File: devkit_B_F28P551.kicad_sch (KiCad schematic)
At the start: 27 parts, among them J1 DEVKIT_C2000_ROW_A, J2 DEVKIT_C2000_ROW_B, J3 Tag-Connect-2050_10, J4 RESET, U1 TMS320F28P551SG5PM, U2 MCP1700-3302E/TT, U3 MCP1700-3302E/TT

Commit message: Devkit B routé, sérigraphie des connecteurs 2x28 et logo
Placement/routage complet du PCB devkit B (24 empreintes, J1/J2 câblés).
Étiquettes de sérigraphie ajoutées sur les 56 broches des connecteurs
Row A/Row B (canal ADC réel, GPIO, rôle de bus générique, alimentations)
via kipy sur l'instance ouverte, plutôt que les noms spécialisés du
schéma. Logo ajouté (lib/lebel-logo) et fp-lib-table versionné.

Co-Authored-By: Claude Sonnet 5 <noreply@anthropic.com>
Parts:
- removed C7: 2u2, Capacitor_SMD:C_0805_2012Metric, symbol Device:C
- removed C9: 100n, Capacitor_SMD:C_0805_2012Metric, symbol Device:C
- renumbered J3 to JTAG1
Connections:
- net GND: now also J1.1 (GND), J1.10 (GND), J1.13 (GND), J1.16 (GND), J1.19 (GND), J1.21 (GND), J1.23 (GND), J1.4 (GND), J1.7 (GND), J2.1 (GND), J2.14 (GND), J2.9 (GND)
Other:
- moved on the sheet: C1, C10, C11, C12, C13, C14, C2, C3, C4, C5, C6, C8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

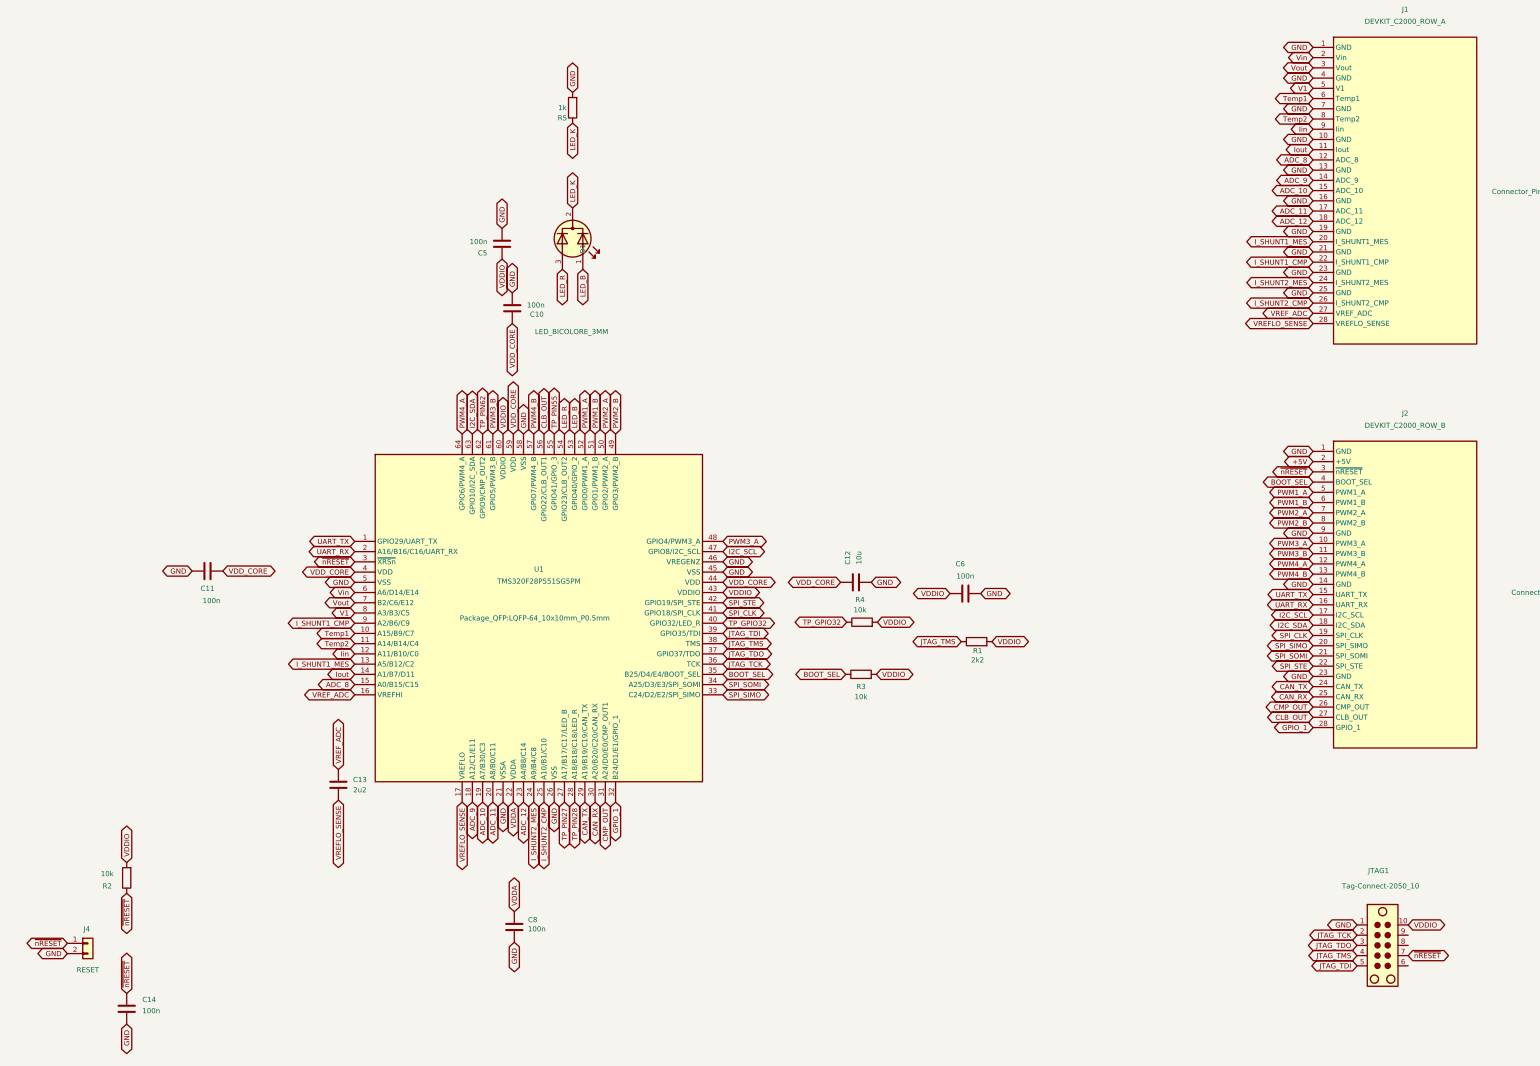
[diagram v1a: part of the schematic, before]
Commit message: devkit_B_F28P551 : rangee A reroutee pour le CLB (Stage1_EN/Stage2_EN/HV_EN/Discharge), documentation rattrapee
Carte figee, production-ready, modifiee malgre la regle habituelle (decision
explicite de l'utilisateur) : miroir de la decision #20 du depot
KICAD-C2000-powershield cote devkit.

- Rangee A reroutee : Stage1_EN (A23, broche 62/GPIO9), Stage2_EN (A24,
  broche 27/GPIO20), HV_EN (A25, broche 28/GPIO21), Discharge (A26, broche
  55/GPIO41) - six masses pour vingt-deux signaux au lieu de dix pour
  dix-huit.
- Rangee B : nRESET -> ~{RESET} (B3), GPIO_1 -> ~{FAULT_MCU} (B28), logique
  negative, meme net.
- devkit_A_F280037 non modifie (CLB absent du F280037) : le connecteur
  n'est plus identique entre les deux devkits, divergence documentee a la
  decision #13.
- doc/decisions.md : nouvelle decision #13.
- doc/spec-devkit.md, doc/brochage-devkit.csv : rangee A de devkit_B
  consignee comme bloc divergent, devkit_A_F280037 garde la rangee
  d'origine comme reference.

Verification avant commit : kicad-cli pcb drc sur devkit_B_F28P551.kicad_pcb
(0 violation, 0 non connecte) ; kicad-cli sch erc (35 violations, 10
erreurs/25 avertissements, toutes de type deja rencontre ailleurs dans
l'atelier - endpoint_off_grid, pin_not_connected -, aucune nouvelle
categorie).

Co-Authored-By: Claude Sonnet 5 <noreply@anthropic.com>
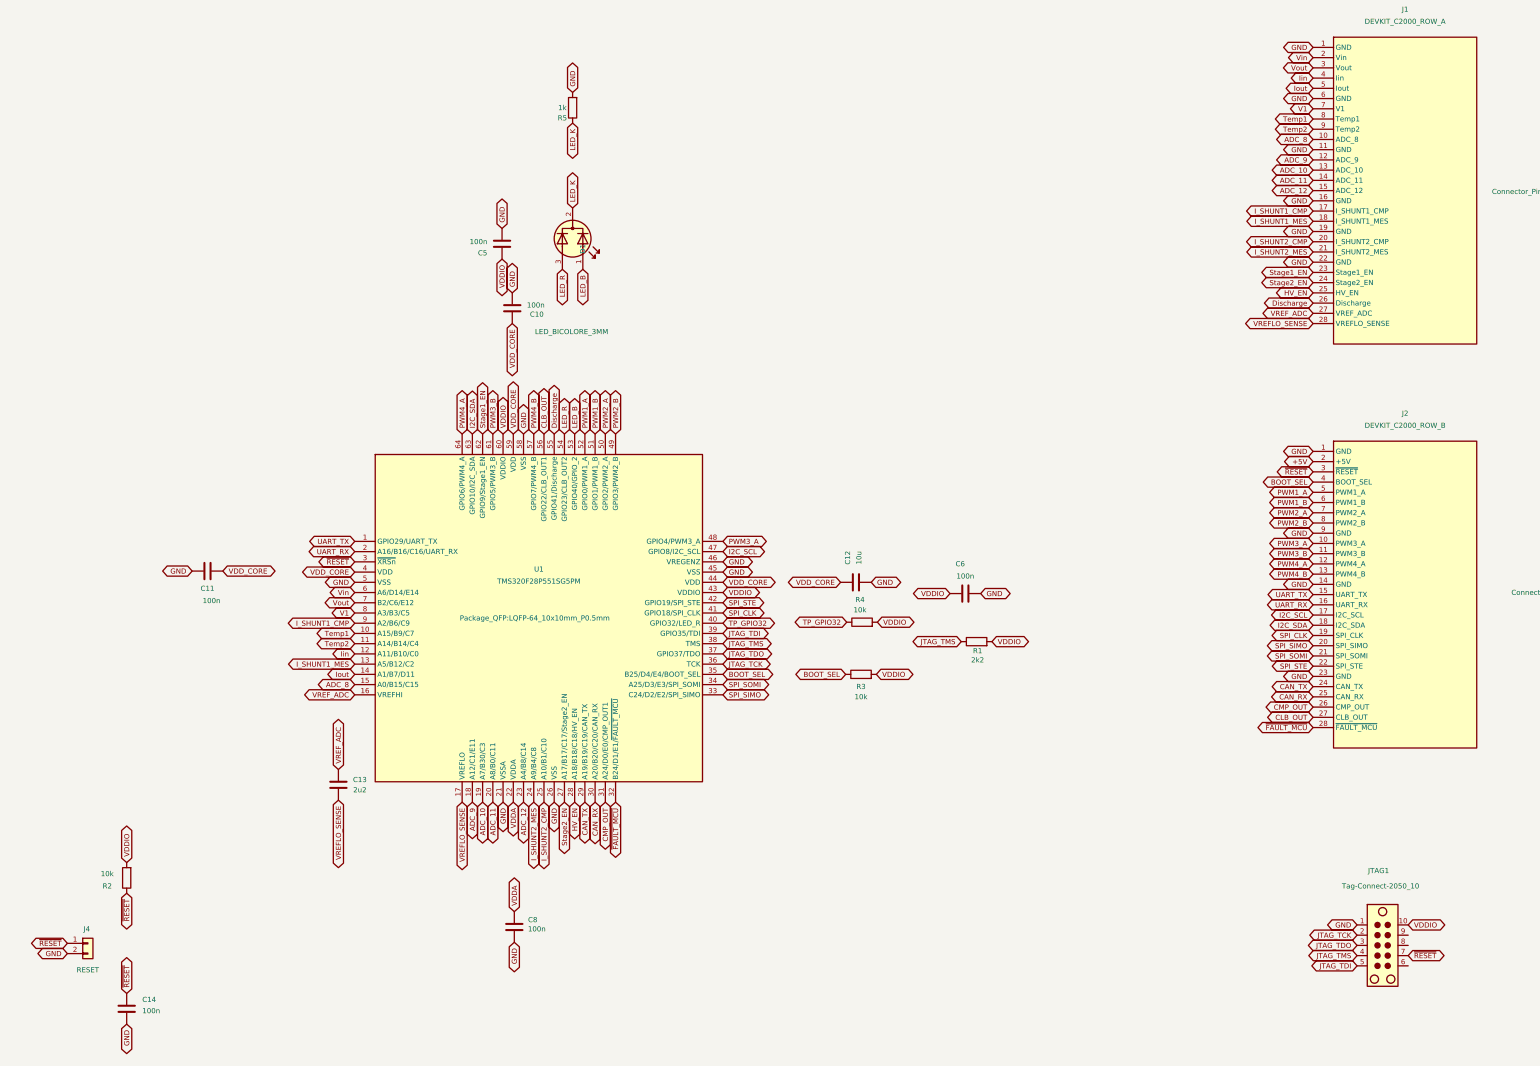
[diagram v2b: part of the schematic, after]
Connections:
- net ADC_10: now also J1.13 (ADC_10); no longer J1.15 (ADC_10)
- net ADC_11: now also J1.14 (ADC_11); no longer J1.17 (ADC_11)
- net ADC_12: now also J1.15 (ADC_12); no longer J1.18 (ADC_12)
- net ADC_8: now also J1.10 (ADC_8); no longer J1.12 (ADC_8)
- net ADC_9: now also J1.12 (ADC_9); no longer J1.14 (ADC_9)
- net GND: now also J1.11 (GND), J1.22 (GND), J1.6 (GND); no longer J1.10 (GND), J1.13 (GND), J1.21 (GND), J1.23 (GND), J1.25 (GND), J1.4 (GND), J1.7 (GND)
- net I_SHUNT1_CMP: now also J1.17 (I_SHUNT1_CMP); no longer J1.22 (I_SHUNT1_CMP)
- net I_SHUNT1_MES: now also J1.18 (I_SHUNT1_MES); no longer J1.20 (I_SHUNT1_MES)
- net I_SHUNT2_CMP: now also J1.20 (I_SHUNT2_CMP); no longer J1.26 (I_SHUNT2_CMP)
- net I_SHUNT2_MES: now also J1.21 (I_SHUNT2_MES); no longer J1.24 (I_SHUNT2_MES)
- net Iin: now also J1.4 (Iin); no longer J1.9 (Iin)
- net Iout: now also J1.5 (Iout); no longer J1.11 (Iout)
- net Temp1: now also J1.8 (Temp1); no longer J1.6 (Temp1)
- net Temp2: now also J1.9 (Temp2); no longer J1.8 (Temp2)
- net V1: now also J1.7 (V1); no longer J1.5 (V1)
- net GPIO_1 renamed ~{FAULT_MCU}
- net TP_PIN27 renamed Stage2_EN
- net Stage2_EN: now also J1.24 (Stage2_EN)
- net TP_PIN28 renamed HV_EN
- net HV_EN: now also J1.25 (HV_EN)
- net TP_PIN55 renamed Discharge
- net Discharge: now also J1.26 (Discharge)
- net TP_PIN62 renamed Stage1_EN
- net Stage1_EN: now also J1.23 (Stage1_EN)
- net ~{nRESET} renamed ~{RESET}

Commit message: Ajoute le connecteur RKB2SJM250SMTR_LFS et partage TO252
- Connecteur RKB2SJM250SMTR_LFS (lib + modele 3D) integre au connecteur
  devkit, modification de brochage associee (modificatio_brochage_devkit)
  -- travail deja en place localement, jamais commite.
- fp-lib-table : empreinte TO252 partagee enregistree
  (lib_fp_commun/TO252.pretty, voir KICAD.md), pas encore utilisee par
  un composant de ce depot.

Co-Authored-By: Claude Sonnet 5 <noreply@anthropic.com>
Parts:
- removed J1: DEVKIT_C2000_ROW_A, Connector_PinHeader_2.54mm:PinHeader_1x28_P2.54mm_Vertical, symbol C2000_Devkit_Connectors:DEVKIT_C2000_ROW_A
- removed J2: DEVKIT_C2000_ROW_B, Connector_PinHeader_2.54mm:PinHeader_1x28_P2.54mm_Vertical, symbol C2000_Devkit_Connectors:DEVKIT_C2000_ROW_B
- removed J4: RESET, Connector_PinHeader_2.54mm:PinHeader_1x02_P2.54mm_Vertical, symbol Connector_Generic:Conn_01x02
- added J1: DEVKIT_C2000_A, Connector_PinHeader_2.54mm:PinHeader_2x24_P2.54mm_Vertical, symbol C2000_Devkit_Connectors:DEVKIT_C2000_A
- added J2: DEVKIT_C2000_B, Connector_PinHeader_2.54mm:PinHeader_2x24_P2.54mm_Vertical, symbol C2000_Devkit_Connectors:DEVKIT_C2000_B
- added S1: RKB2SJM250SMTR_LFS, lib:RKB2SJM250SMTRLFS, symbol RKB2SJM250SMTR_LFS:RKB2SJM250SMTR_LFS
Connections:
- net +5V: now also J2.2 (+5V)
- net ADC_10: now also J1.20 (ADC_10)
- net ADC_11: now also J1.21 (ADC_11)
- net ADC_12: now also J1.24 (ADC_12)
- net ADC_8: now also J1.16 (ADC_8)
- net ADC_9: now also J1.17 (ADC_9)
- net BOOT_SEL: now also J2.6 (BOOT_SEL)
- net CAN_RX: now also J2.42 (CAN_RX)
- net CAN_TX: now also J2.39 (CAN_TX)
- net CLB_OUT: now also J2.46 (CLB_OUT)
- net CMP_OUT: now also J2.43 (CMP_OUT)
- net Discharge: now also J1.40 (Discharge)
- net GND: now also J1.10 (GND), J1.11 (GND), J1.14 (GND), J1.15 (GND), J1.18 (GND), J1.19 (GND), J1.2 (GND), J1.22 (GND), J1.23 (GND), J1.26 (GND), J1.27 (GND), J1.3 (GND), J1.30 (GND), J1.31 (GND), J1.34 (GND), J1.35 (GND), J1.38 (GND), J1.39 (GND), J1.42 (GND), J1.43 (GND), J1.46 (GND), J1.6 (GND), J1.7 (GND), J2.1 (GND), J2.12 (GND), J2.13 (GND), J2.16 (GND), J2.17 (GND), J2.20 (GND), J2.21 (GND), J2.24 (GND), J2.25 (GND), J2.28 (GND), J2.29 (GND), J2.32 (GND), J2.33 (GND), J2.36 (GND), J2.37 (GND), J2.4 (GND), J2.40 (GND), J2.41 (GND), J2.44 (GND), J2.45 (GND), J2.48 (GND), J2.5 (GND), J2.8 (GND), J2.9 (GND), S1.3 (NO_1), S1.4 (NO_2)
- net HV_EN: now also J1.37 (HV_EN)
- net I2C_SCL: now also J2.27 (I2C_SCL)
- net I2C_SDA: now also J2.30 (I2C_SDA)
- net I_SHUNT1_CMP: now also J1.25 (I_SHUNT1_CMP)
- net I_SHUNT1_MES: now also J1.28 (I_SHUNT1_MES)
- net I_SHUNT2_CMP: now also J1.29 (I_SHUNT2_CMP)
- net I_SHUNT2_MES: now also J1.32 (I_SHUNT2_MES)
- net Iin: now also J1.5 (Iin)
- net Iout: now also J1.8 (Iout)
- net PWM1_A: now also J2.7 (PWM1_A)
- net PWM1_B: now also J2.10 (PWM1_B)
- net PWM2_A: now also J2.11 (PWM2_A)
- net PWM2_B: now also J2.14 (PWM2_B)
- net PWM3_A: now also J2.15 (PWM3_A)
- net PWM3_B: now also J2.18 (PWM3_B)
- net PWM4_A: now also J2.19 (PWM4_A)
- net PWM4_B: now also J2.22 (PWM4_B)
- net SPI_CLK: now also J2.31 (SPI_CLK)
- net SPI_SIMO: now also J2.34 (SPI_SIMO)
- net SPI_SOMI: now also J2.35 (SPI_SOMI)
- net SPI_STE: now also J2.38 (SPI_STE)
- net Stage1_EN: now also J1.33 (Stage1_EN)
- net Stage2_EN: now also J1.36 (Stage2_EN)
- net Temp1: now also J1.12 (Temp1)
- net Temp2: now also J1.13 (Temp2)
- net UART_RX: now also J2.26 (UART_RX)
- net UART_TX: now also J2.23 (UART_TX)
- net V1: now also J1.9 (V1)
- net VREFLO_SENSE: now also J1.45 (VREFLO_SENSE)
- net VREF_ADC: now also J1.44 (VREF_ADC)
- net Vin: now also J1.1 (Vin)
- net Vout: now also J1.4 (Vout)
- net ~{FAULT_MCU}: now also J1.41 (~{FAULT_MCU})
- net ~{RESET}: now also J2.3 (~{RESET}), S1.1 (COM_1), S1.2 (COM_2)
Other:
- moved on the sheet: C14
